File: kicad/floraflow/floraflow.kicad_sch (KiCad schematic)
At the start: 14 parts, among them M1 Water valve 1, M2 Water valve 2, M3 Water valve 3, M4 Water valve 4, M5 Water valve 5, M6 Water valve 6, M7 Water valve 7, M8 Water valve 8, U1 230VAC-12VDC switched PSU, U2 12V-5V DC-DC converter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

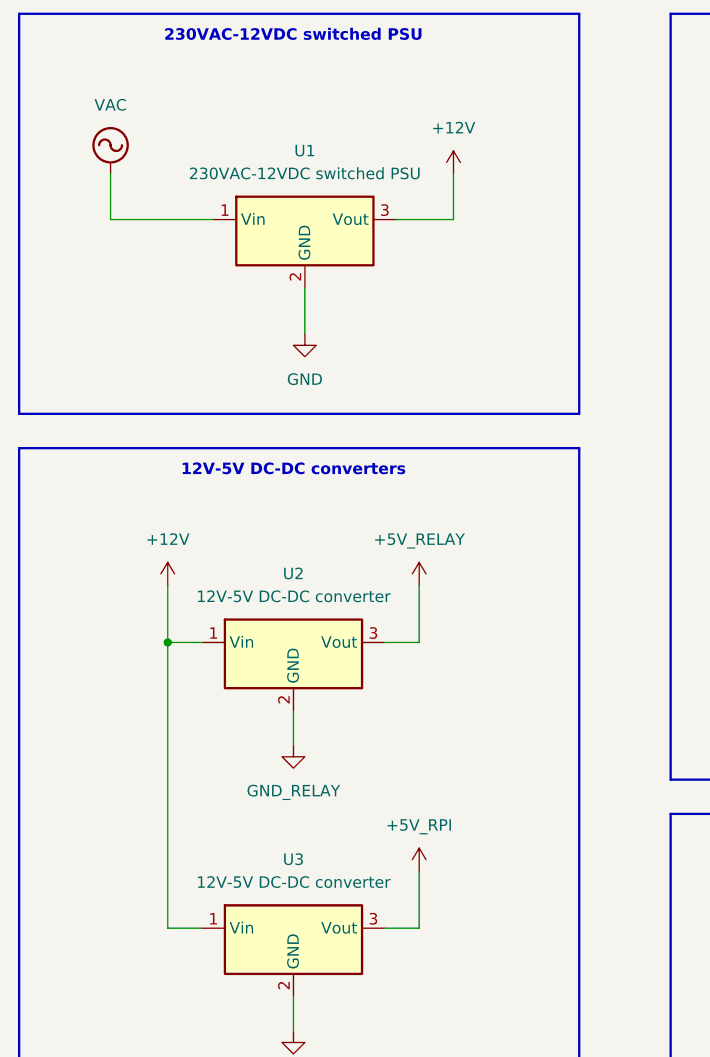
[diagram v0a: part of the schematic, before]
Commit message: doc: add example column in bom list, update wiring schematic and image
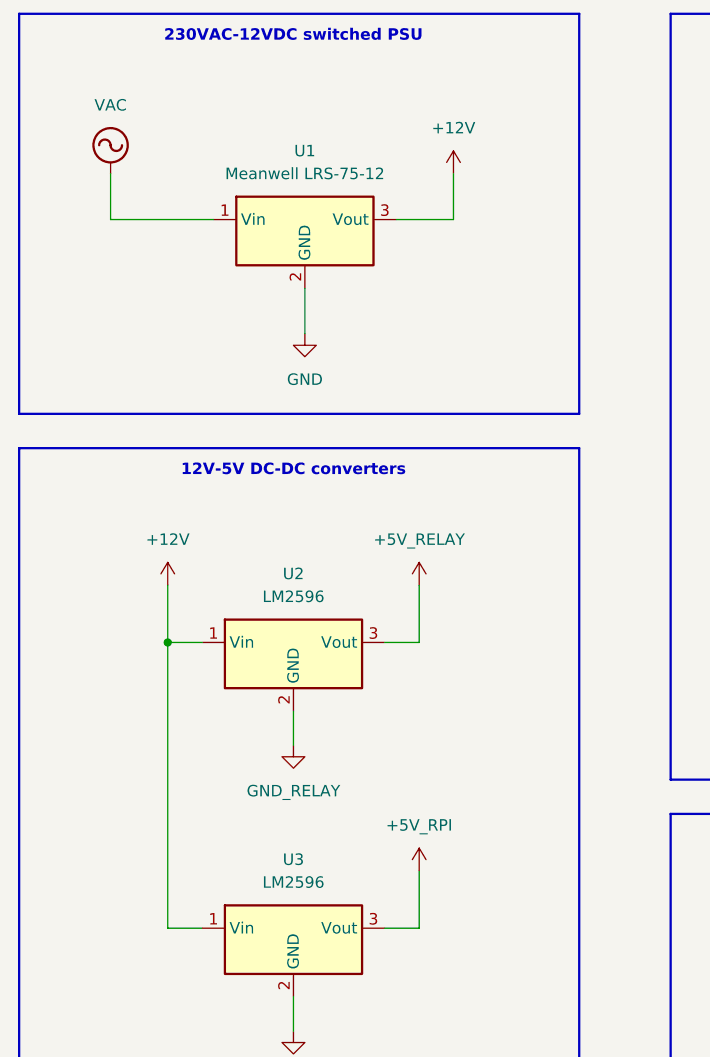
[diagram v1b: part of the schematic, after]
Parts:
- U1: value 230VAC-12VDC switched PSU -> Meanwell LRS-75-12
- U2, U3: value 12V-5V DC-DC converter -> LM2596
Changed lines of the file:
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@@
 			)
 		)
-		(property "Value" "12V-5V DC-DC converter"
+		(property "Value" "LM2596"
 			(at 46.99 80.01 0)
 			(show_name no)
@@
 			)
 		)
-		(property "Value" "12V-5V DC-DC converter"
+		(property "Value" "LM2596"
 			(at 46.99 111.76 0)
 			(show_name no)
@@
 			)
 		)
-		(property "Value" "230VAC-12VDC switched PSU"
+		(property "Value" "Meanwell LRS-75-12"
 			(at 48.26 33.02 0)
 			(show_name no)
